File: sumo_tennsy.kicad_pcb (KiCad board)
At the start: 4 copper layers, 80 x 50 mm, 47 parts, among them J1 CONN_01X03, J10 TB_1X2, J11 TB_1X2, J12 HEADER_2, J13 HEADER_2, J14 TB_1X2, J15 HEADER_2, J16 HEADER_2, J17 CONN_01X03, J2 CONN_01X03, J3 CONN_01X03, J4 CONN_01X03, J5 CONN_01X03, J6 CONN_01X03, J7 CONN_01X03, J8 CONN_01X03, J9 HEADER_4, P1 HEADER_02X05, P2 HEADER_02X05, Q1 2N7002, U1 Teensy4.0, U2 MCP2515-xSO, U3 TJA1050, U4 LM1117-SOT

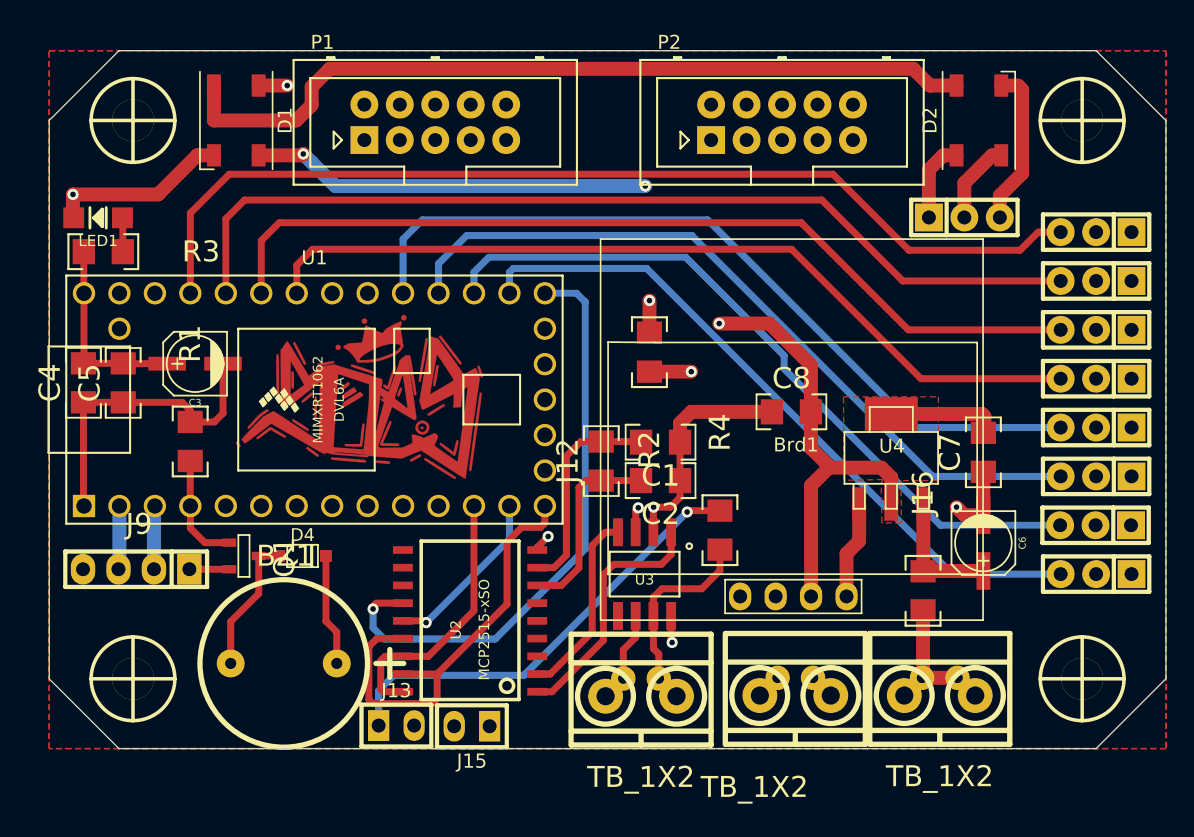
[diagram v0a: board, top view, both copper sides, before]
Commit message: modifcaciones
se agrego vista 3d y se modifico pcb
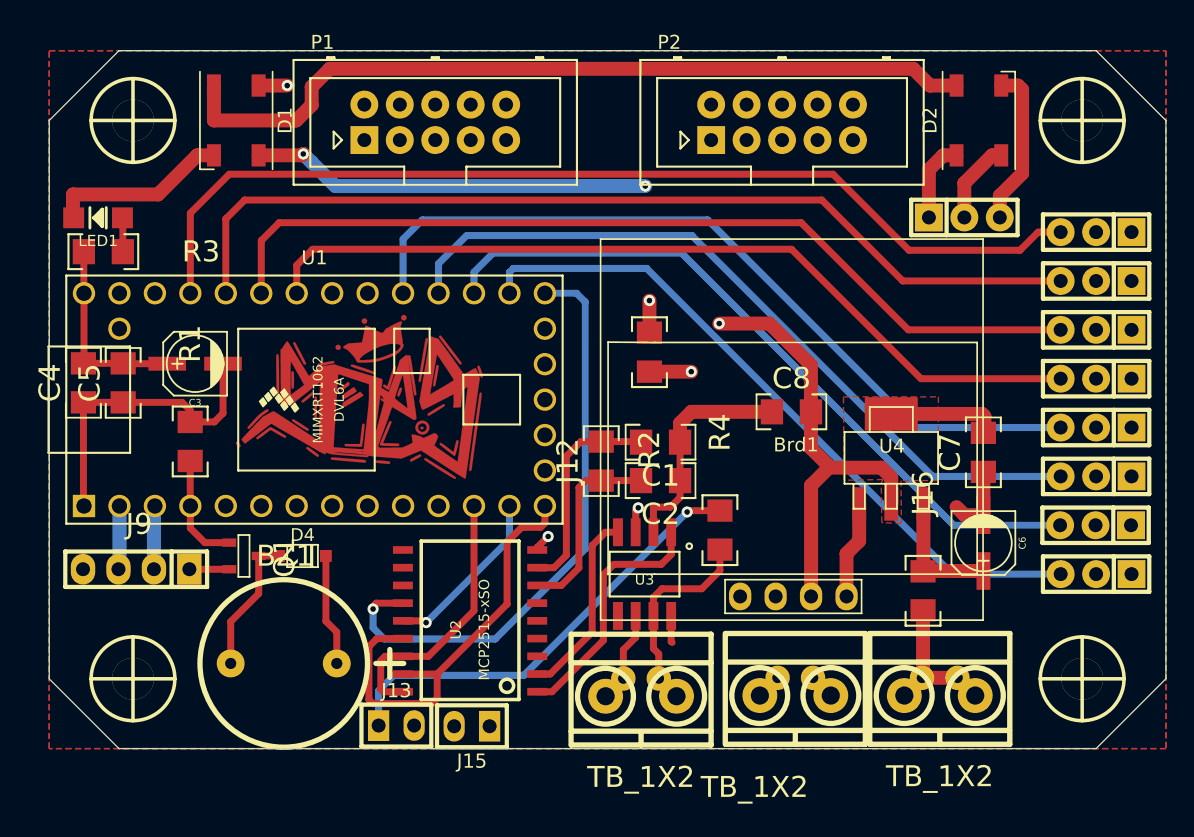
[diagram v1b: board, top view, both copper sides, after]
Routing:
- net GND: vias 5 -> 1
- added copper zone on B.Cu, net GND
- added copper zone on F.Cu, net GND
- removed copper zone on B.Cu, net (none)
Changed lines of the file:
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@@
-(kicad_pcb (version 20171130) (host pcbnew 5.1.7-a382d34a8~87~ubuntu20.04.1)
+(kicad_pcb (version 20171130) (host pcbnew "(5.1.4)-1")
   (general
     (thickness 1.6)
     (drawings 15)
-    (tracks 309)
+    (tracks 303)
     (zones 0)
     (modules 47)
@@
   )
   (setup
-    (last_trace_width 1)
+    (last_trace_width 0.25)
     (user_trace_width 0.5)
     (user_trace_width 0.75)
@@
     (pad_to_mask_clearance 0)
     (aux_axis_origin 0 0)
-    (visible_elements FFFFFF7F)
+    (visible_elements 7FFFFFFF)
     (pcbplotparams
       (layerselection 0x010fc_ffffffff)
@@
     (pad 2 thru_hole oval (at -1.08 -10.6 270) (size 2 1.6) (drill 1) (layers *.Cu *.Mask)
       (net 5 +5V))
+    (model ${KISYS3DMOD}/128x64_I2C_OLEDDisplay_Adafruit.wrl
+      (at (xyz 0 0 0))
+      (scale (xyz 1 1 1))
+      (rotate (xyz 0 0 0))
+    )
   )
   (module EESTN5:hole_3mm (layer F.Cu)
@@
   (segment (start 110.0425 107.1525) (end 110.04 107.15) (width 0.5) (layer F.Cu) (net 3) (status 30))
   (segment (start 112.89336 107.1525) (end 110.0425 107.1525) (width 0.5) (layer F.Cu) (net 3) (status 30))
-  (via (at 143.3 102.7) (size 0.8) (drill 0.4) (layers F.Cu B.Cu) (net 3))
   (segment (start 143.285 102.715) (end 143.3 102.7) (width 0.5) (layer F.Cu) (net 3))
   (segment (start 143.285 104.5) (end 143.285 102.715) (width 0.5) (layer F.Cu) (net 3) (status 10))
@@
   (segment (start 111.825 96.6) (end 110.1 96.6) (width 0.5) (layer F.Cu) (net 3) (status 20))
   (segment (start 112.45 95.975) (end 111.825 96.6) (width 0.5) (layer F.Cu) (net 3))
-  (via (at 101.7 80.3) (size 0.8) (drill 0.4) (layers F.Cu B.Cu) (net 3))
   (segment (start 157.12 109.1) (end 157.12 106.03) (width 1) (layer F.Cu) (net 3) (status 10))
   (segment (start 158.025 105.125) (end 158.025 102.475) (width 1) (layer F.Cu) (net 3) (status 20))
   (segment (start 157.12 106.03) (end 158.025 105.125) (width 1) (layer F.Cu) (net 3))
   (segment (start 166.925 100.172) (end 166.925 103.275) (width 1) (layer F.Cu) (net 3) (status 30))
-  (via (at 165 102.7) (size 0.8) (drill 0.4) (layers F.Cu B.Cu) (net 3))
   (segment (start 165.575 103.275) (end 165 102.7) (width 1) (layer F.Cu) (net 3))
   (segment (start 166.925 103.275) (end 165.575 103.275) (width 1) (layer F.Cu) (net 3) (status 10))
@@
   (segment (start 145.194 96.681) (end 145.194 98.05) (width 1) (layer F.Cu) (net 3) (status 20))
   (segment (start 146 95.875) (end 145.194 96.681) (width 1) (layer F.Cu) (net 3))
-  (via (at 144.625 112.4) (size 0.8) (drill 0.4) (layers F.Cu B.Cu) (net 3))
   (segment (start 144.555 110.5) (end 144.555 112.33) (width 0.5) (layer F.Cu) (net 3) (status 10))
   (segment (start 144.555 112.33) (end 144.625 112.4) (width 0.5) (layer F.Cu) (net 3))
@@
   (segment (start 142.015 104.5) (end 142.015 102.93501) (width 0.5) (layer F.Cu) (net 5) (status 10))
   (segment (start 142.015 102.93501) (end 142.20001 102.75) (width 0.5) (layer F.Cu) (net 5))
-  (segment (start 122.81 84.59) (end 122.81 87.38) (width 1) (layer E.Cu) (net 11) (status 20))
-  (segment (start 124 83.4) (end 122.81 84.59) (width 1) (layer E.Cu) (net 11))
-  (segment (start 143.6 83.4) (end 124 83.4) (width 1) (layer E.Cu) (net 11))
-  (segment (start 149.5 89.3) (end 143.6 83.4) (width 1) (layer E.Cu) (net 11))
-  (segment (start 149.5 109.1) (end 149.5 89.3) (width 1) (layer E.Cu) (net 11) (status 10))
-  (segment (start 141.1 105.475) (end 141.1 76.43293) (width 1) (layer A.Cu) (net 13))
-  (segment (start 138.532071 73.865001) (end 132.735001 73.865001) (width 1) (layer A.Cu) (net 13) (status 20))
-  (segment (start 138.65 107.925) (end 141.1 105.475) (width 1) (layer A.Cu) (net 13))
-  (segment (start 126.125 107.925) (end 138.65 107.925) (width 1) (layer A.Cu) (net 13))
-  (segment (start 141.1 76.43293) (end 138.532071 73.865001) (width 1) (layer A.Cu) (net 13))
-  (segment (start 125.35 102.62) (end 125.35 107.15) (width 1) (layer A.Cu) (net 13) (status 10))
-  (segment (start 125.35 107.15) (end 126.125 107.925) (width 1) (layer A.Cu) (net 13))
-  (segment (start 127.89 105.34) (end 127.89 102.62) (width 1) (layer A.Cu) (net 14) (status 20))
-  (segment (start 139.075 104.675) (end 137.45 106.3) (width 1) (layer A.Cu) (net 14))
-  (segment (start 139.075 78.975) (end 139.075 104.675) (width 1) (layer A.Cu) (net 14))
-  (segment (start 136.505001 76.405001) (end 139.075 78.975) (width 1) (layer A.Cu) (net 14))
-  (segment (start 128.85 106.3) (end 127.89 105.34) (width 1) (layer A.Cu) (net 14))
-  (segment (start 137.45 106.3) (end 128.85 106.3) (width 1) (layer A.Cu) (net 14))
-  (segment (start 132.735001 76.405001) (end 136.505001 76.405001) (width 1) (layer A.Cu) (net 14) (status 10))
   (segment (start 155.05 76.440002) (end 155.085001 76.405001) (width 1) (layer A.Cu) (net 5) (status 30))
   (segment (start 154.569 95.875) (end 154.569 92.519) (width 1) (layer F.Cu) (net 5))
@@
   (segment (start 167 97.303) (end 167 96.2) (width 1) (layer F.Cu) (net 5))
   (segment (start 166.925 97.378) (end 167 97.303) (width 1) (layer F.Cu) (net 5))
-  (segment (start 163.85 104) (end 172.42 104) (width 0.5) (layer B.Cu) (net 6))
-  (segment (start 152.65 92.8) (end 163.85 104) (width 0.5) (layer B.Cu) (net 6))
-  (segment (start 152.65 91.85) (end 152.65 92.8) (width 0.5) (layer B.Cu) (net 6))
-  (segment (start 145.6 84.8) (end 152.65 91.85) (width 0.5) (layer B.Cu) (net 6))
-  (segment (start 131.5 84.8) (end 145.6 84.8) (width 0.5) (layer B.Cu) (net 6))
-  (segment (start 130.43 85.87) (end 131.5 84.8) (width 0.5) (layer B.Cu) (net 6))
+  (segment (start 164.8 104) (end 172.42 104) (width 0.5) (layer B.Cu) (net 6))
+  (segment (start 145.3 84.5) (end 164.8 104) (width 0.5) (layer B.Cu) (net 6))
+  (segment (start 131.8 84.5) (end 145.3 84.5) (width 0.5) (layer B.Cu) (net 6))
   (segment (start 130.43 87.38) (end 130.43 85.87) (width 0.5) (layer B.Cu) (net 6))
+  (segment (start 130.43 85.87) (end 131.8 84.5) (width 0.5) (layer B.Cu) (net 6))
   (segment (start 146.05 83.25) (end 129.9 83.25) (width 0.5) (layer B.Cu) (net 7))
   (segment (start 172.46 100.5) (end 163.3 100.5) (width 0.5) (layer B.Cu) (net 7) (status 10))
@@
   (segment (start 161.55 90) (end 153.875 82.325) (width 0.5) (layer F.Cu) (net 10))
   (segment (start 172.46 90) (end 161.55 90) (width 0.5) (layer F.Cu) (net 10))
+  (segment (start 122.81 84.59) (end 122.81 87.38) (width 1) (layer E.Cu) (net 11) (status 20))
+  (segment (start 124 83.4) (end 122.81 84.59) (width 1) (layer E.Cu) (net 11))
+  (segment (start 143.6 83.4) (end 124 83.4) (width 1) (layer E.Cu) (net 11))
+  (segment (start 149.5 89.3) (end 143.6 83.4) (width 1) (layer E.Cu) (net 11))
+  (segment (start 149.5 109.1) (end 149.5 89.3) (width 1) (layer E.Cu) (net 11) (status 10))
   (segment (start 152.04 88.44) (end 152.04 109.1) (width 1) (layer E.Cu) (net 12) (status 20))
   (segment (start 144.9 81.3) (end 152.04 88.44) (width 1) (layer E.Cu) (net 12))
@@
   (segment (start 120.27 83.63) (end 122.6 81.3) (width 1) (layer E.Cu) (net 12))
   (segment (start 120.27 87.38) (end 120.27 83.63) (width 1) (layer E.Cu) (net 12))
+  (segment (start 141.1 105.475) (end 141.1 76.43293) (width 1) (layer A.Cu) (net 13))
+  (segment (start 138.532071 73.865001) (end 132.735001 73.865001) (width 1) (layer A.Cu) (net 13) (status 20))
+  (segment (start 138.65 107.925) (end 141.1 105.475) (width 1) (layer A.Cu) (net 13))
+  (segment (start 126.125 107.925) (end 138.65 107.925) (width 1) (layer A.Cu) (net 13))
+  (segment (start 141.1 76.43293) (end 138.532071 73.865001) (width 1) (layer A.Cu) (net 13))
+  (segment (start 125.35 102.62) (end 125.35 107.15) (width 1) (layer A.Cu) (net 13) (status 10))
+  (segment (start 125.35 107.15) (end 126.125 107.925) (width 1) (layer A.Cu) (net 13))
+  (segment (start 127.89 105.34) (end 127.89 102.62) (width 1) (layer A.Cu) (net 14) (status 20))
+  (segment (start 139.075 104.675) (end 137.45 106.3) (width 1) (layer A.Cu) (net 14))
+  (segment (start 139.075 78.975) (end 139.075 104.675) (width 1) (layer A.Cu) (net 14))
+  (segment (start 136.505001 76.405001) (end 139.075 78.975) (width 1) (layer A.Cu) (net 14))
+  (segment (start 128.85 106.3) (end 127.89 105.34) (width 1) (layer A.Cu) (net 14))
+  (segment (start 137.45 106.3) (end 128.85 106.3) (width 1) (layer A.Cu) (net 14))
+  (segment (start 132.735001 76.405001) (end 136.505001 76.405001) (width 1) (layer A.Cu) (net 14) (status 10))
   (segment (start 125.1 109.875) (end 122.81 107.585) (width 1) (layer A.Cu) (net 15))
   (segment (start 141.775 109.875) (end 125.1 109.875) (width 1) (layer A.Cu) (net 15))
@@
     )
   )
-  (zone (net 0) (net_name "") (layer F.Cu) (hatch edge 0.508)
+  (zone (net 3) (net_name GND) (layer F.Cu) (hatch edge 0.508)
     (connect_pads yes (clearance 0.608))
     (min_thickness 0.254)
@@
     )
   )
-  (zone (net 0) (net_name "") (layer B.Cu) (hatch edge 0.508)
+  (zone (net 3) (net_name GND) (layer B.Cu) (hatch edge 0.508)
     (connect_pads yes (clearance 0.608))
     (min_thickness 0.254)
